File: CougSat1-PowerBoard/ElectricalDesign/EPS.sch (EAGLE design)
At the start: 428 parts, among them J1 Deployable 0, J10 Battery -, J11 PGND, J12 Battery +, J13 VBatt, J2 PV0, J3 PV1, J4 Umbilical, J5 CougSat Card, J6 SWD, J7 PV2, J8 PV3, J9 Deployable 1, Q1 CSD25402Q3A, Q10 CSD25402Q3A, Q11 DMN53D0LDW, Q12 CSD25402Q3A, Q13 DMN53D0LDW, Q14 CSD25402Q3A, Q15 DMN53D0LDW, Q16 CSD25402Q3A, Q17 CSD25402Q3A, Q18 CSD25402Q3A, Q19 DMN53D0LDW, Q2 DMN2008LFU, Q20 CSD25402Q3A, Q21 CSD25402Q3A, Q22 CSD25402Q3A, Q23 DMN53D0LDW, Q24 CSD25402Q3A, Q25 DMN53D0LDW, Q26 CSD25402Q3A, Q27 DMN53D0LDW, Q28 CSD25402Q3A, Q29 CSD25402Q3A, Q3 DMN2008LFU, Q30 CSD25402Q3A, Q31 DMN53D0LDW, Q32 CSD25402Q3A, Q33 DMN53D0LDW, Q34 CSD25402Q3A, Q35 CSD25402Q3A, Q36 DMN53D0LDW, Q37 CSD25402Q3A, Q38 CSD25402Q3A, Q39 DMN53D0LDW, Q4 CSD25402Q3A, Q40 CSD25402Q3A, Q41 CSD25402Q3A, Q42 DMN53D0LDW, Q43 CSD25402Q3A, Q5 DMN53D0LDW, Q6 DMN53D0LDW, Q7 CSD25402Q3A, Q8 CSD25402Q3A, Q9 CSD25402Q3A, SW1 ESE24MH1, U1 INA199C2, U10 INA199C2, U11 INA199C1, U12 AD7689, U13 INA199C2, U14 INA199C2, U15 TXS0102DQM, U16 TXS0102DQM, U17 AD8515, U18 BQ29700, U19 INA199C2, U2 AD7689, U20 TXS0102DQM, U21 TXS0102DQM, U22 STM32L476RGT, U23 AD7291, U24 INA199C2, U25 INA199C2, U26 BQ29700, U27 INA199C2, U28 INA199C2, U29 INA199C2, U3 AD8515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

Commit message: Adjusted notes
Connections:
- new net CHASSIS_RBF0: C55.1, H4.MOUNT, R34.2
- new net CHASSIS_RBF1: C77.1, H3.MOUNT, R48.2
- net CHASSIS: no longer C55.1, C77.1, H3.MOUNT, H4.MOUNT, R34.2, R48.2
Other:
- note added: "Addr=0x20 (7b)"
- note added: "Addr=0x2B (7b)"
- note added: "Addr=0x2C (7b)"
- note added: "Addr=0x2E (7b)"
- note added: "Addr=0x2F (7b)"
- note added: "Separation Switch (NC)"
- note removed: "Addr=0x40|R/!W"
- note removed: "Addr=0x56|R/!W"
- note removed: "Addr=0x58|R/!W"
- note removed: "Addr=0x5C|R/!W"
- note removed: "Addr=0x5E|R/!W"
- note removed: "Deployment Switch"
- moved on the sheet: RT10, RT14

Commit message: Added power inhibit page
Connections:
- net BATTERY-: now also C61.2, C67.2, D11.GND, J4.3, J4.4
- net PGND: no longer C61.2, C67.2, D11.GND, J4.3, J4.4
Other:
- note added: "Cell Protection"
- note added: "Loads"
- note added: "Page 10"
- note added: "Page 10: PMIC Page 11: SPI ADCs Page 12: I²C ADCs Page 13: Mechanical Layout"
- note added: "Page 11, 12"
- note added: "Page 1: Block Diagram Page 2: Power Rails Page 3: Power Inhibits Page 4: Input Switching Page 5: Batteries Page 6: 3.3V Regulation Page 7: Output Switching Page 8: Output Switching Page 9: Backplane Connections"
- note added: "Page 6"
- note added: "Pages 7, 8"
- note added: "Separation Switch"
- note added: "Umbilical Charger"
- note removed: "Page 10, 11"
- note removed: "Page 10: SPI ADCs Page 11: I²C ADCs Page 12: Mechanical Layout"
- note removed: "Page 1: Block Diagram Page 2: Power Rails Page 3: Input Switching Page 4: Batteries Page 5: 3.3V Regulation Page 6: Output Switching Page 7: Output Switching Page 8: Backplane Connections Page 9: PMIC"
- note removed: "Page 3"
- note removed: "Page 3, 8"
- note removed: "Page 6, 10"
- note removed: "Pages 6, 7, 8"

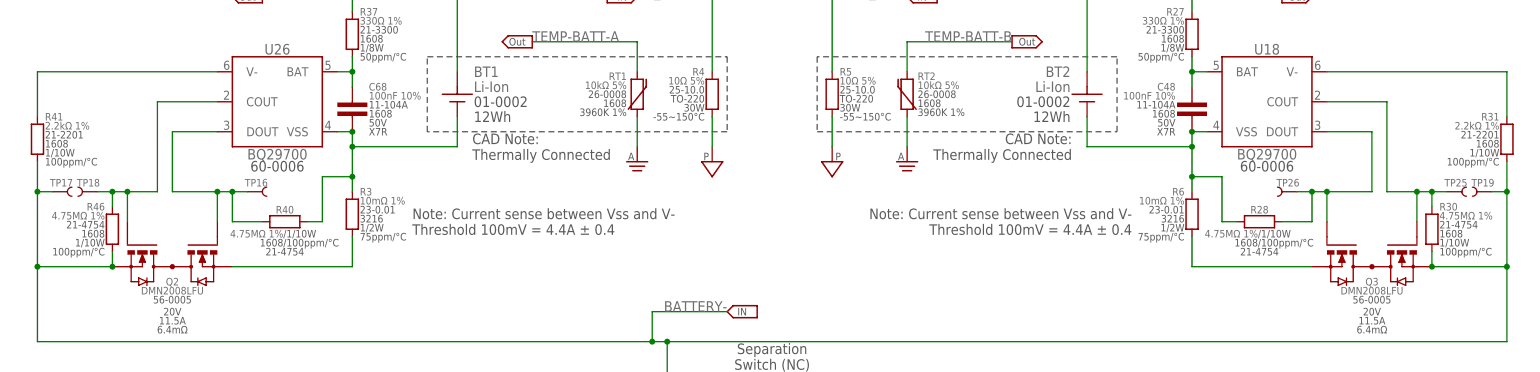
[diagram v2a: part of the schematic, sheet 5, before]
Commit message: Removed unhelpful copper
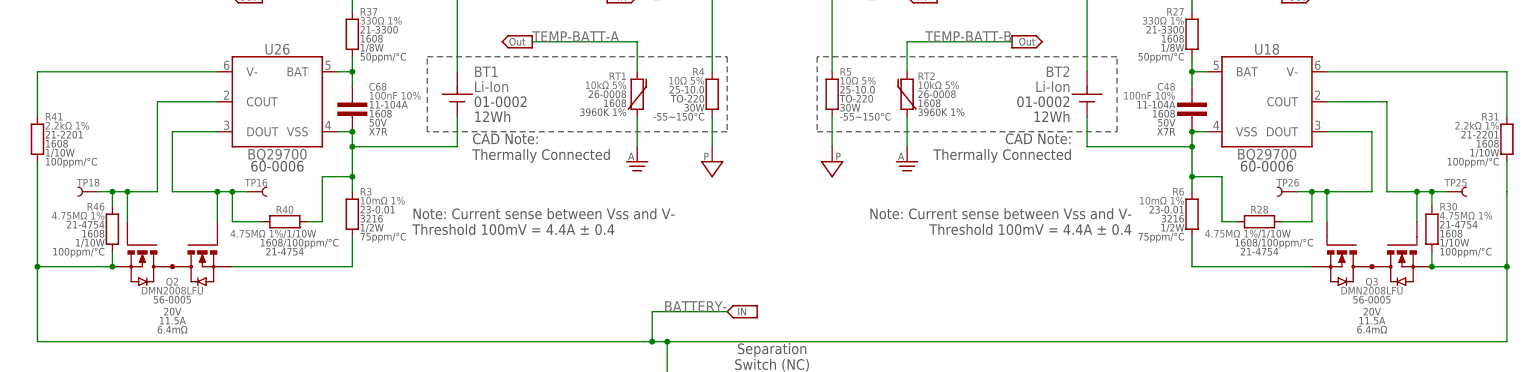
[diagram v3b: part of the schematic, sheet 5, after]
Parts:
- removed TP17, TP19: TEST_POINT-THT-1.0, CougsInSpace-Connectors:TEST_POINT-THT-1.0
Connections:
- net BATTERY-: no longer TP17.1, TP19.1
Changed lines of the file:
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@@
 <part name="OFFSHEET214" library="CougsInSpace-Aesthetics" deviceset="OFF_SHEET-IN" device=""/>
 <part name="OFFSHEET218" library="CougsInSpace-Aesthetics" deviceset="OFF_SHEET-IN" device=""/>
-<part name="TP19" library="CougsInSpace-Connectors" deviceset="TEST_POINT" device="-THT-1.0" value="TEST_POINT-THT-1.0"/>
-<part name="TP17" library="CougsInSpace-Connectors" deviceset="TEST_POINT" device="-THT-1.0" value="TEST_POINT-THT-1.0"/>
 <part name="Y2" library="CougsInSpace-Clocks" deviceset="CRYSTAL" device="-SMD-3215" technology="-32.768K" value="32.768kHz ±10ppm"/>
 <part name="Y1" library="CougsInSpace-Clocks" deviceset="CRYSTAL-GROUNDED" device="-SMD-5032" technology="-8M" value="8MHz ±10ppm"/>
@@
 <attribute name="RDS" x="231.14" y="62.992" size="1.27" layer="97" align="center"/>
 </instance>
-<instance part="TP19" gate="G$1" x="251.46" y="86.36" smashed="yes">
-<attribute name="NAME" x="249.936" y="87.884" size="1.27" layer="95" align="center"/>
-</instance>
-<instance part="TP17" gate="G$1" x="7.62" y="86.36" smashed="yes" rot="MR0">
-<attribute name="NAME" x="9.144" y="87.884" size="1.27" layer="95" rot="MR0" align="center"/>
-</instance>
 <instance part="R8" gate="G$1" x="187.96" y="152.4" smashed="yes" rot="MR0">
 <attribute name="NAME" x="189.23" y="154.432" size="1.27" layer="95" rot="MR0" align="center"/>
@@
 <wire x1="17.78" y1="76.2" x2="17.78" y2="73.66" width="0.1524" layer="91"/>
 <junction x="17.78" y="73.66"/>
-<pinref part="TP17" gate="G$1" pin="1"/>
-<wire x1="7.62" y1="86.36" x2="5.08" y2="86.36" width="0.1524" layer="91"/>
-<junction x="5.08" y="86.36"/>
 <wire x1="5.08" y1="73.66" x2="5.08" y2="60.96" width="0.1524" layer="91"/>
 <wire x1="5.08" y1="60.96" x2="109.22" y2="60.96" width="0.1524" layer="91"/>
@@
 <pinref part="Q3" gate="G$1" pin="S2"/>
 <junction x="241.3" y="73.66"/>
-<pinref part="TP19" gate="G$1" pin="1"/>
-<wire x1="251.46" y1="86.36" x2="254" y2="86.36" width="0.1524" layer="91"/>
-<junction x="254" y="86.36"/>
 <wire x1="109.22" y1="60.96" x2="111.76" y2="60.96" width="0.1524" layer="91"/>
 <wire x1="111.76" y1="60.96" x2="254" y2="60.96" width="0.1524" layer="91"/>

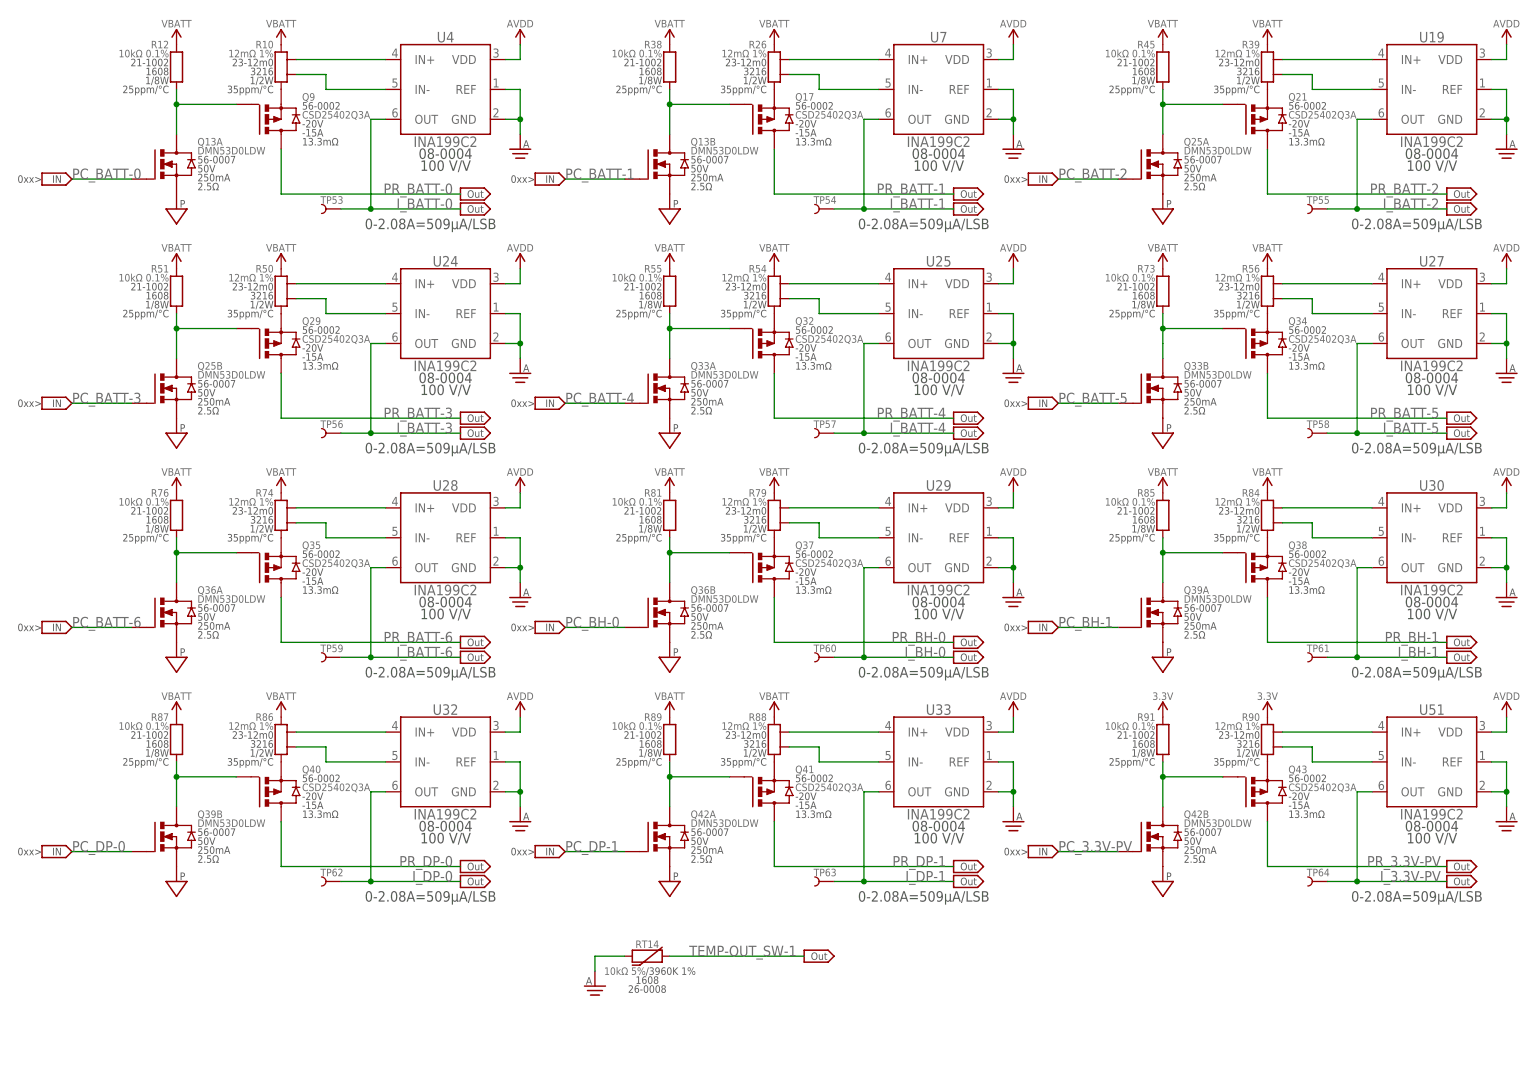
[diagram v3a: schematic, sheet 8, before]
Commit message: Laid out output switching
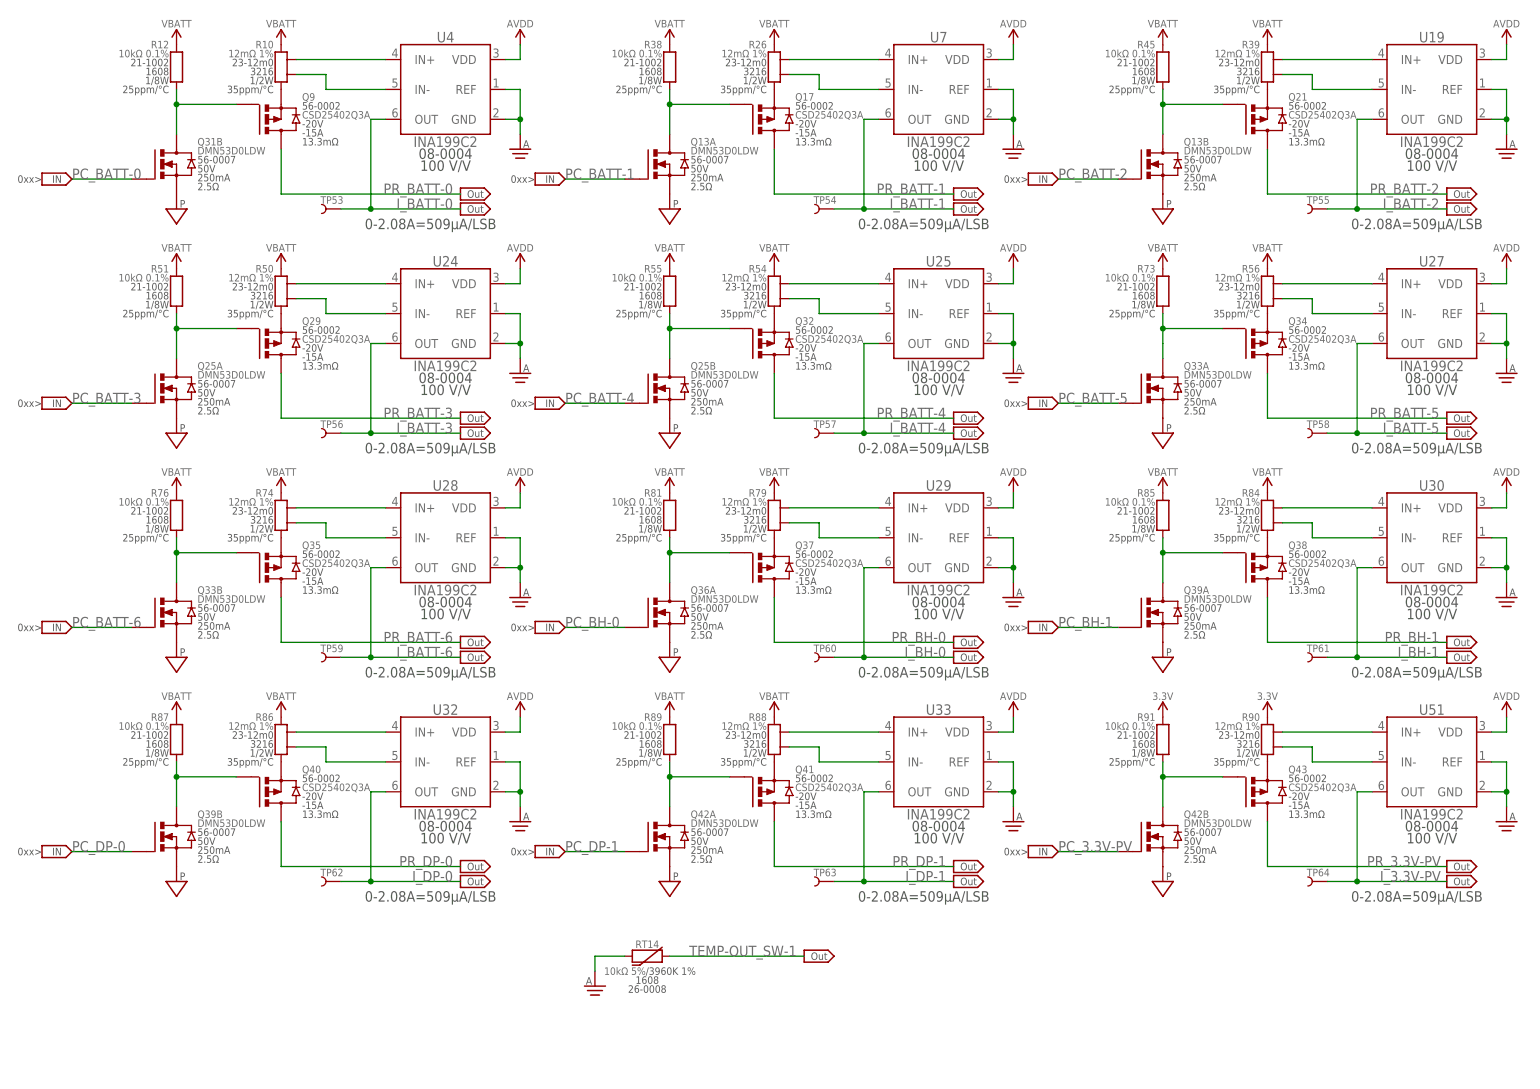
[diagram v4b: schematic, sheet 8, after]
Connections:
- net !PC_BATT-0: now also Q31B.D; no longer Q13A.D
- net !PC_BATT-1: now also Q13A.D; no longer Q13B.D
- net !PC_BATT-2: now also Q13B.D; no longer Q25A.D
- net !PC_BATT-3: now also Q25A.D; no longer Q25B.D
- net !PC_BATT-4: now also Q25B.D; no longer Q33A.D
- net !PC_BATT-5: now also Q33A.D; no longer Q33B.D
- net !PC_BATT-6: now also Q33B.D; no longer Q36A.D
- net !PC_BH-0: now also Q36A.D; no longer Q36B.D
- net PC_BATT-0: now also Q31B.G; no longer Q13A.G
- net PC_BATT-1: now also Q13A.G; no longer Q13B.G
- net PC_BATT-2: now also Q13B.G; no longer Q25A.G
- net PC_BATT-3: now also Q25A.G; no longer Q25B.G
- net PC_BATT-4: now also Q25B.G; no longer Q33A.G
- net PC_BATT-5: now also Q33A.G; no longer Q33B.G
- net PC_BATT-6: now also Q33B.G; no longer Q36A.G
- net PC_BH-0: now also Q36A.G; no longer Q36B.G
- net PGND: now also Q31B.S; no longer Q36B.S
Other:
- moved on the sheet: Q13A, Q13B, Q25A, Q25B, Q33A, Q33B, Q36A
